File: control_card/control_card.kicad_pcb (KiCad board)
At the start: 2 copper layers, 27 parts, among them IC1 TLSR8253F512ET48, J1 Conn_02x04_Counter_Clockwise, U1 Wifi, Y1 Crystal_GND24_Small

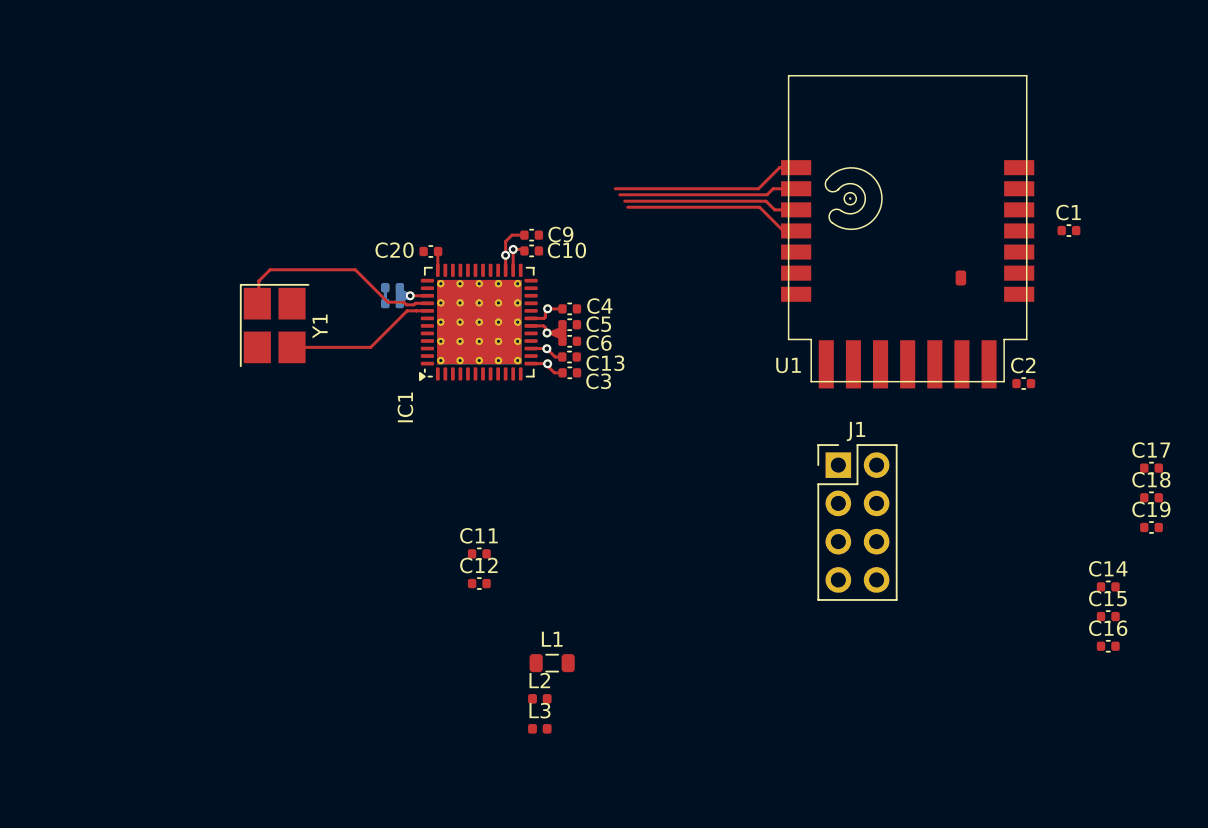
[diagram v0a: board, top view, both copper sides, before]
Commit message: PCB : started footprint and rooting
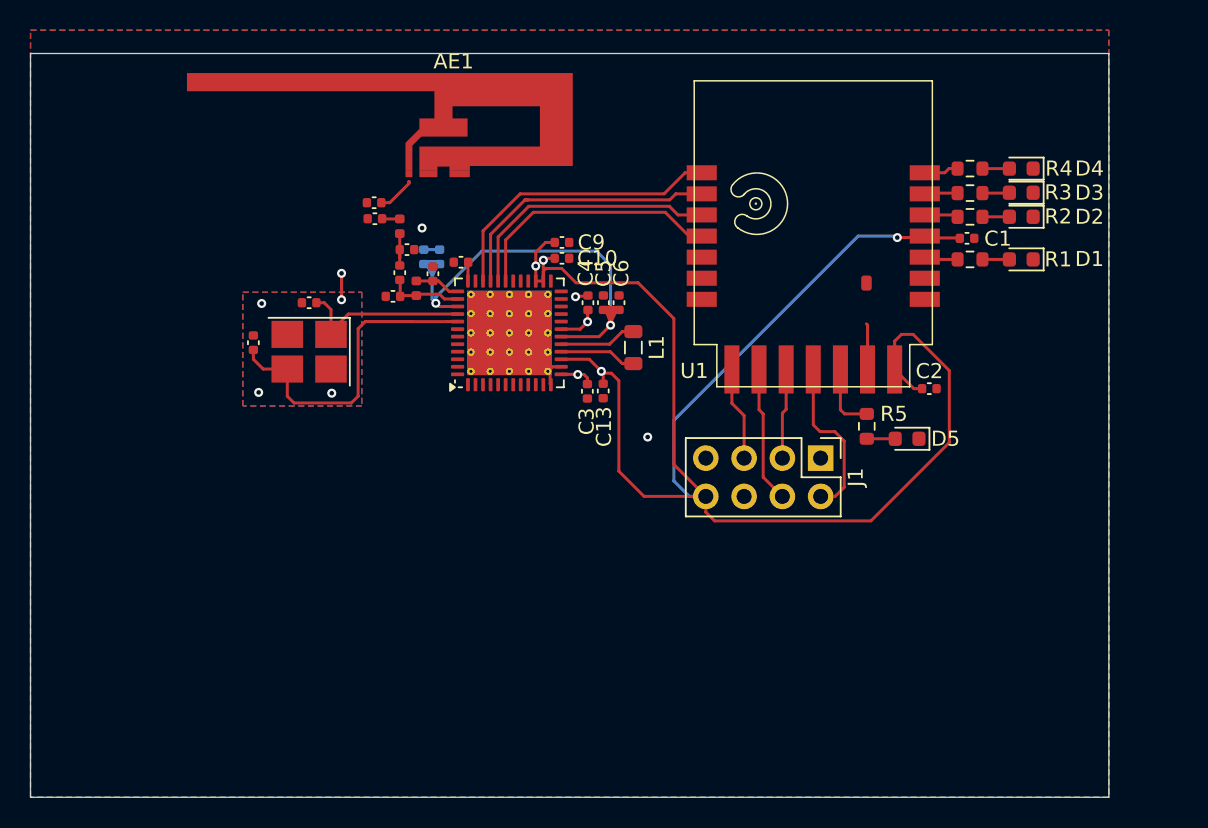
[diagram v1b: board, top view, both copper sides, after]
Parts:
- added AE1: Antenna, Footprint_Rang_Dong:Antenna, F.Cu at (73.0, 71.1)
- added D1: LED, LED_SMD:LED_0603_1608Metric, F.Cu at (110.6, 80.0)
- added D2: LED, LED_SMD:LED_0603_1608Metric, F.Cu at (110.6, 77.1)
- added D3: LED, LED_SMD:LED_0603_1608Metric, F.Cu at (110.6, 75.5)
- added D4: LED, LED_SMD:LED_0603_1608Metric, F.Cu at (110.6, 73.9)
- added D5: LED, LED_SMD:LED_0603_1608Metric, F.Cu at (103.1, 91.9)
- added R1: R, Resistor_SMD:R_0603_1608Metric, F.Cu at (107.2, 80.0)
- added R2: R, Resistor_SMD:R_0603_1608Metric, F.Cu at (107.2, 77.1)
- added R3: R, Resistor_SMD:R_0603_1608Metric, F.Cu at (107.2, 75.6)
- added R4: R, Resistor_SMD:R_0603_1608Metric, F.Cu at (107.2, 73.9)
- added R5: R, Resistor_SMD:R_0603_1608Metric, F.Cu at (100.4, 91.0)
- moved C19 55.9 mm to (67.7, 76.2), turned to 180 degrees
- moved C18 54.8 mm to (67.8, 77.3), turned to 180 degrees
- moved C16 53.1 mm to (69.4, 80.8), turned to 90 degrees
- moved C15 52.0 mm to (69.0, 82.4), turned to 180 degrees
- moved C17 51.5 mm to (69.9, 79.3)
- moved C14 49.4 mm to (71.6, 80.9), turned to 90 degrees
- moved L3 34.6 mm to (69.4, 77.8), turned to 90 degrees
- moved L2 28.4 mm to (70.5, 81.9), turned to 90 degrees
- moved C12 21.9 mm to (59.7, 85.5), turned to 90 degrees
- moved L1 21.6 mm to (84.9, 85.8), turned to -90 degrees
- moved C11 20.1 mm to (63.4, 82.8), turned to 180 degrees
- moved C1 6.78 mm to (107.0, 78.6)
- moved C2 6.27 mm to (104.5, 88.5)
- moved U1 6.27 mm to (88.9, 68.1)
- moved C8 4.40 mm to (72.0, 79.8), turned to 90 degrees
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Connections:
- net ANTENNA renamed Net-(AE1-A)
- U1 pad 10: CT1 -> CT3
- U1 pad 11: CT1 -> CT4
- U1 pad 9: CT1 -> CT2
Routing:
- net +3.3V: track 7.81 -> 111.3 mm, vias 3 -> 4
- net +1V2: track 6.13 -> 27.4 mm
- net Clock2: track 9.89 -> 21.3 mm
- net CT4: track 0.00 -> 11.1 mm
- net GND: track 0.00 -> 10.3 mm, vias 0 -> 8
- net CT2: track 0.00 -> 9.07 mm
- net In_1: track 12.6 -> 19.4 mm
- net In_2: track 11.9 -> 18.4 mm
- net CT1: track 0.00 -> 6.22 mm
- net CT3: track 0.00 -> 5.99 mm
- net In_3: track 11.6 -> 17.5 mm
- net In_4: track 11.8 -> 17.2 mm
- net Net-(IC1-VDCDC): track 0.00 -> 5.13 mm
- net Net-(IC1-VDCDC_SW): track 0.00 -> 5.11 mm
- net ANT: track 0.00 -> 5.10 mm
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- added copper zone on B.Cu, net GND
- added copper zone on F.Cu, net GND
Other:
- board outline added: 71.6 x 49.4 mm

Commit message: PCB (control_card): Almost Finished
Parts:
- AE1: value Antenna -> Antenna_Shield
- D1, D2, D3, D4, D5: footprint LED_SMD:LED_0603_1608Metric -> LED_SMD:LED_0805_2012Metric
- J1: moved to B.Cu
- moved J1 72.5 mm to (109.2, 21.6), turned to 90 degrees
- moved D5 61.3 mm to (89.2, 32.1), turned to 0 degrees
- moved R5 59.4 mm to (92.5, 32.1), turned to 180 degrees
- moved C15 51.8 mm to (73.4, 30.8), turned to 0 degrees
- moved U1 51.3 mm to (116.3, 24.7), turned to -90 degrees
- moved C16 50.6 mm to (71.9, 30.3)
- moved C18 50.6 mm to (71.4, 26.8)
- moved C19 50.6 mm to (71.4, 25.8)
- moved D1 50.5 mm to (89.2, 34.2), turned to 0 degrees
- moved L2 50.2 mm to (72.4, 31.8), turned to 0 degrees
- moved Y1 50.1 mm to (67.7, 36.2), turned to -90 degrees
- moved C17 49.7 mm to (73.4, 29.8)
- moved C2 49.6 mm to (96.7, 39.6), turned to 180 degrees
- moved L3 49.5 mm to (71.9, 28.3)
- moved C14 49.2 mm to (74.3, 31.8), turned to 0 degrees
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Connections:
- R1 pad 1: Led_1 -> Led_4
- R2 pad 1: Led_2 -> Led_3
- R3 pad 1: Led_3 -> Led_2
- R4 pad 1: Led_4 -> Led_1
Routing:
- net +3.3V: track 111.3 -> 156.5 mm, vias 4 -> 7
- net In_1: track 19.4 -> 40.1 mm, vias 0 -> 2
- net In_2: track 18.4 -> 38.3 mm, vias 0 -> 2
- net Led_4: track 2.29 -> 21.2 mm, vias 0 -> 2
- net In_3: track 17.5 -> 36.3 mm, vias 0 -> 2
- net In_4: track 17.2 -> 34.5 mm, vias 0 -> 2
- net CT4: track 11.1 -> 27.6 mm
- net Led_3: track 2.20 -> 18.7 mm, vias 0 -> 2
- net Led_2: track 2.23 -> 17.2 mm, vias 0 -> 2
- net Led_1: track 2.24 -> 14.6 mm, vias 0 -> 2
- net CT3: track 5.99 -> 17.2 mm
- net CT2: track 9.07 -> 17.8 mm
- net Clock2: track 21.3 -> 14.7 mm, vias 0 -> 2
- net CT1: track 6.22 -> 12.6 mm
- net GND: track 10.3 -> 5.25 mm, vias 8 -> 7
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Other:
- board size 71.6 x 49.4 mm -> 55.5 x 25.5 mm

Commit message: PCB (control_card) : V1 finished
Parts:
- moved C19 5.26 mm to (76.4, 27.5), turned to -90 degrees
- moved L2 4.68 mm to (70.4, 27.5), turned to -90 degrees
- moved C14 4.63 mm to (70.3, 29.5), turned to -90 degrees
- moved C18 3.95 mm to (75.3, 27.5), turned to -90 degrees
- moved C16 3.21 mm to (71.8, 27.1), turned to 0 degrees
- moved C15 3.02 mm to (71.3, 28.6), turned to -90 degrees
- moved L3 2.29 mm to (73.8, 27.1), turned to 0 degrees
- moved C17 1.62 mm to (72.3, 28.6), turned to -90 degrees
- moved AE1 0.89 mm to (81.6, 23.1)
- moved C11 0.81 mm to (64.9, 36.9)
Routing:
- net GND: track 5.25 -> 29.9 mm, vias 7 -> 11
- net ANT: track 7.72 -> 17.4 mm
- net VANT: track 5.33 -> 13.8 mm
- net Net-(AE1-A): track 2.08 -> 4.83 mm
- net +3.3V: track 156.5 -> 158.3 mm, vias 7 -> 6
- net CT1: track 12.6 -> 13.2 mm, vias 0 -> 1
- net VDD_F: track 2.66 -> 2.74 mm, vias 1 -> 0
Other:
- board size 55.5 x 25.5 mm -> 55.7 x 26.3 mm

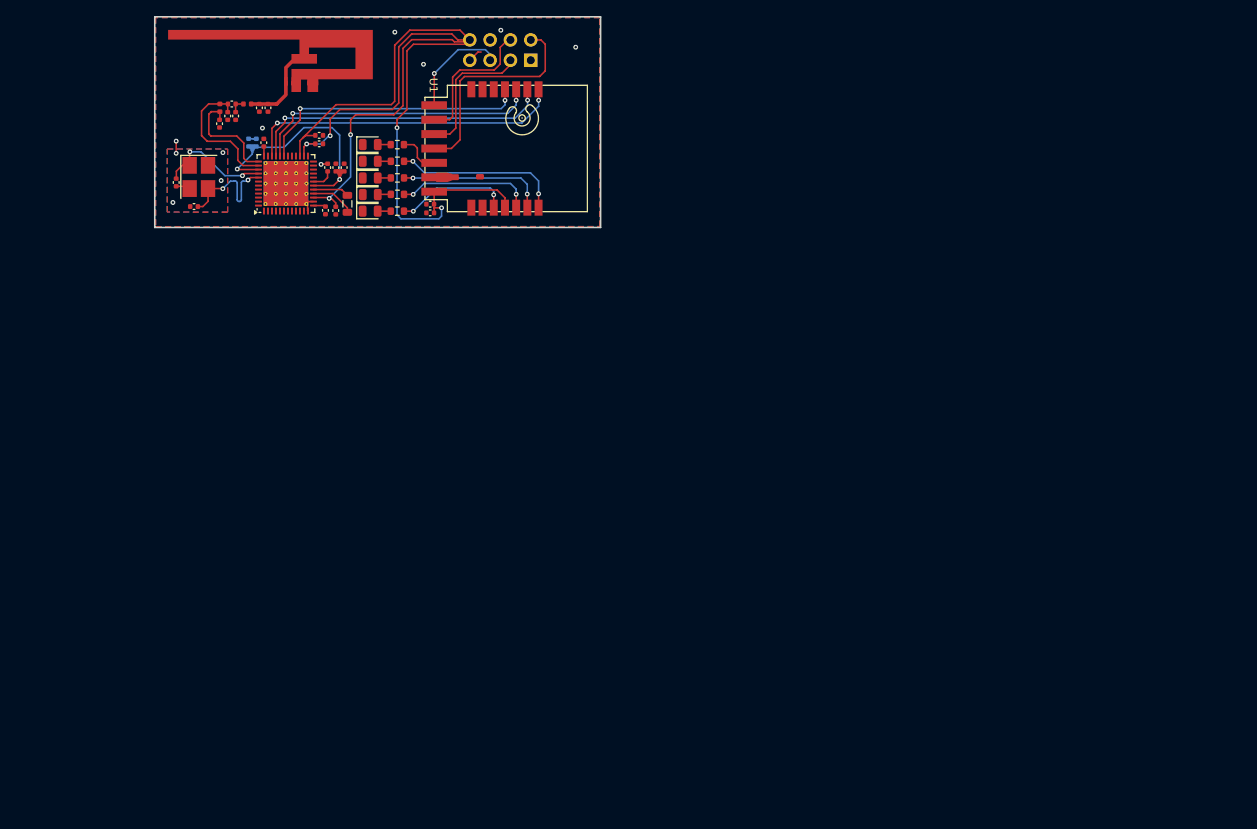
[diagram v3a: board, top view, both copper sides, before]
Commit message: PCB (control_card): V2 almost finished
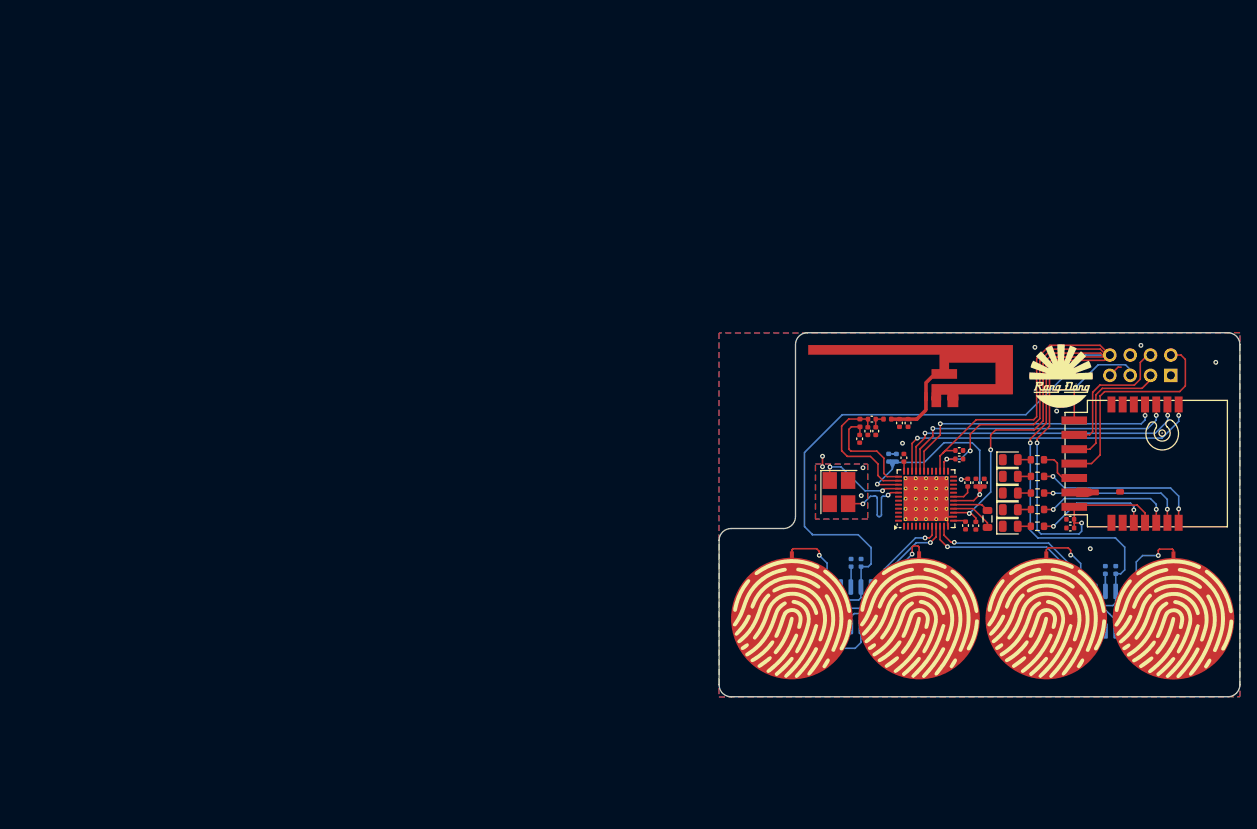
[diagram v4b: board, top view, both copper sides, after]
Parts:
- removed C11, C12: 1µF, Capacitor_SMD:C_0402_1005Metric
- added C21: 10nF, Capacitor_SMD:C_0402_1005Metric, B.Cu at (149.3, 84.4)
- added C22: 0.1µF, Capacitor_SMD:C_0402_1005Metric, B.Cu at (150.5, 84.4)
- added C24: 0.1µF, Capacitor_SMD:C_0402_1005Metric, B.Cu at (182.3, 85.3)
- added C25: 10nF, Capacitor_SMD:C_0402_1005Metric, B.Cu at (181.0, 85.3)
- added G***: LOGO, LOGO, F.Cu at (175.5, 61.1)
- added G***: LOGO, LOGO, F.Cu at (173.7, 91.4)
- added G***: LOGO, LOGO, F.Cu at (189.6, 91.4)
- added G***: LOGO, LOGO, F.Cu at (141.9, 91.4)
- added G***: LOGO, LOGO, F.Cu at (157.8, 91.4)
- added J2: Conn_01x01_Pin, Footprint_Rang_Dong:Touch-Pad, F.Cu at (141.9, 91.4)
- added J3: Conn_01x01_Pin, Footprint_Rang_Dong:Touch-Pad, F.Cu at (173.7, 91.4)
- added J4: Conn_01x01_Pin, Footprint_Rang_Dong:Touch-Pad, F.Cu at (157.8, 91.4)
- added J4: Conn_01x01_Pin, Footprint_Rang_Dong:Touch-Pad, F.Cu at (189.6, 91.4)
- added U2: ~, Package_SO:SOIC-8_3.9x4.9mm_P1.27mm, B.Cu at (149.9, 89.9)
- added U3: ~, Package_SO:SOIC-8_3.9x4.9mm_P1.27mm, B.Cu at (181.7, 90.4)
- moved C14 89.2 mm to (150.3, 68.9)
- moved C16 89.2 mm to (151.9, 66.4)
- moved C10 89.2 mm to (162.8, 71.4)
- moved C17 89.2 mm to (152.3, 67.9)
- moved C18 89.2 mm to (155.3, 66.9)
- moved C20 89.2 mm to (155.9, 71.3)
- moved C4 89.2 mm to (163.8, 74.4)
- moved C5 89.2 mm to (164.9, 74.4)
- moved C6 89.2 mm to (165.9, 74.4)
- moved C7 89.2 mm to (154.0, 71.3)
- moved C8 89.2 mm to (154.9, 71.3)
- moved C9 89.2 mm to (162.8, 70.4)
- moved D4 89.2 mm to (169.2, 79.8)
- moved L1 89.2 mm to (166.3, 78.9)
- moved L2 89.2 mm to (150.4, 66.9)
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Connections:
- IC1 pad 10: unconnected-(IC1-PB0-Pad10) -> Sig_4
- IC1 pad 11: unconnected-(IC1-PB1-Pad11) -> Sig_3
- IC1 pad 8: unconnected-(IC1-PA6-Pad8) -> Sig_2
- IC1 pad 9: unconnected-(IC1-PA7-Pad9) -> Sig_1
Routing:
- net +3.3V: track 158.3 -> 286.0 mm, vias 6 -> 7
- net Sig_3: track 0.00 -> 29.5 mm, vias 0 -> 1
- net Sig_4: track 0.00 -> 28.7 mm, vias 0 -> 1
- net Touch_2: track 0.00 -> 23.1 mm, vias 0 -> 1
- net Sig_2: track 0.00 -> 20.4 mm, vias 0 -> 1
- net Sig_1: track 0.00 -> 19.6 mm, vias 0 -> 1
- net Touch_4: track 0.00 -> 17.5 mm, vias 0 -> 1
- net Touch_3: track 0.00 -> 15.6 mm, vias 0 -> 1
- net Touch_1: track 0.00 -> 14.1 mm, vias 0 -> 1
- net Clock2: track 14.7 -> 11.6 mm
- net Clock1: track 14.7 -> 11.8 mm
- net Net-(U2-VC): track 0.00 -> 2.56 mm
- net Net-(U3-VC): track 0.00 -> 2.20 mm
- net GND: track 29.9 -> 28.3 mm
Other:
- board size 55.7 x 26.3 mm -> 65.1 x 45.5 mm

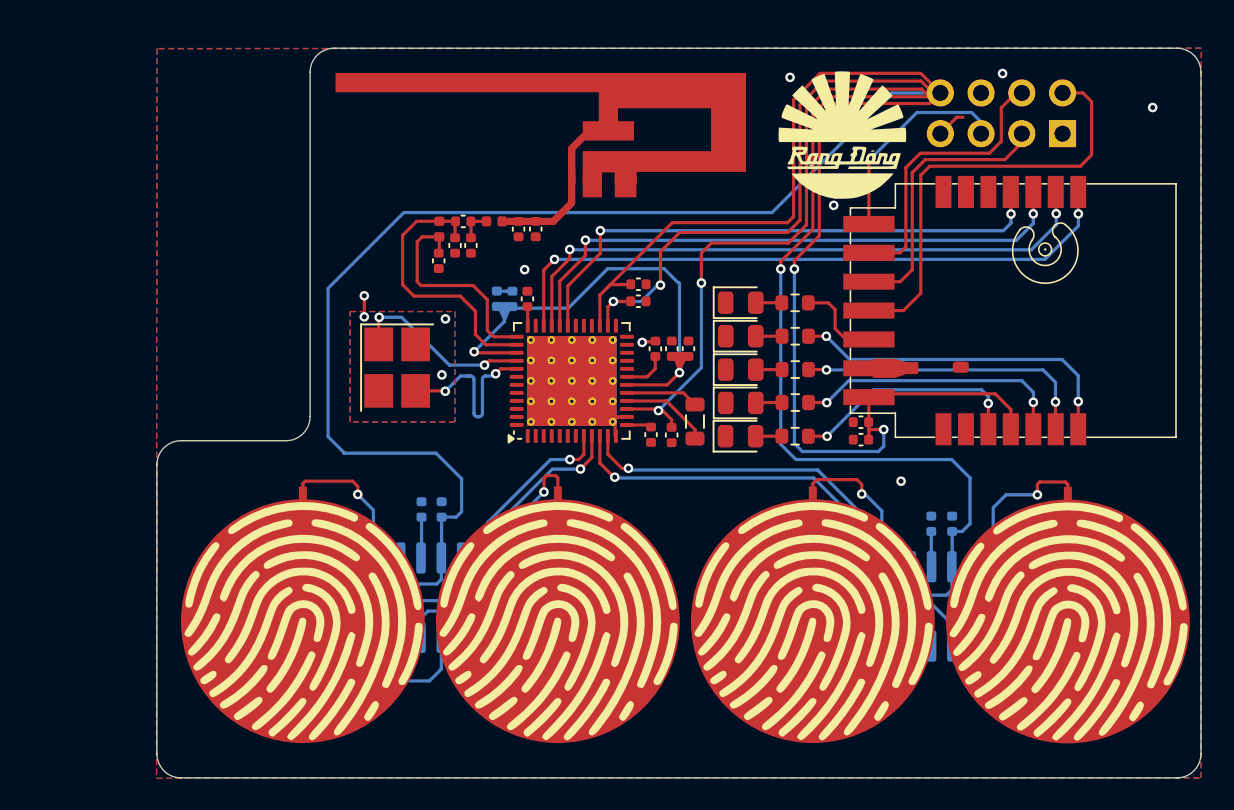
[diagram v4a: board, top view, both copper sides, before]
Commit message: PCB (control_card) : V3 finished, perfect dimension
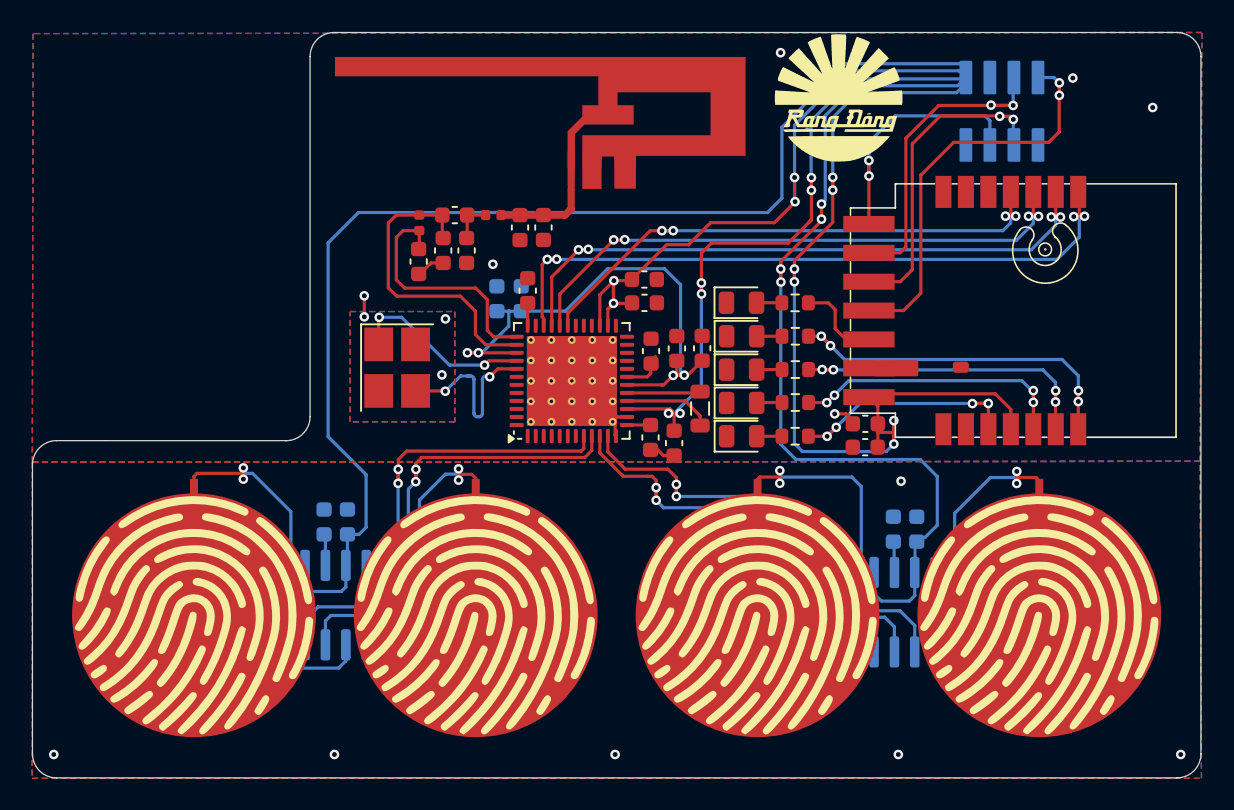
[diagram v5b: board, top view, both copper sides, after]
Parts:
- removed the G*** at (173.7, 91.4)
- removed the G*** at (189.6, 91.4)
- removed the G*** at (141.9, 91.4)
- removed the G*** at (157.8, 91.4)
- C1, C10, C13, C14, C15, C16, C17, C18, C19, C2, C20, C21, C22, C24, C25, C3, C4, C5, C6, C7, C8, C9: footprint Capacitor_SMD:C_0402_1005Metric -> Capacitor_SMD:C_0603_1608Metric
- J1: footprint Connector_PinHeader_2.54mm:PinHeader_2x04_P2.54mm_Vertical -> Footprint_Rang_Dong:Male connector
- moved J2 6.80 mm to (135.1, 91.0)
- moved C21 6.13 mm to (143.2, 85.2)
- moved U2 5.97 mm to (143.9, 90.4)
- moved C22 5.92 mm to (144.6, 85.2)
- moved J4 5.13 mm to (152.6, 91.0)
- moved J3 3.47 mm to (170.2, 91.0)
- moved C25 2.39 mm to (178.7, 85.6)
- moved U3 2.34 mm to (179.4, 90.8)
- moved G*** 2.33 mm to (175.3, 58.8)
- moved C24 2.23 mm to (180.1, 85.6)
- moved J5 1.82 mm to (187.8, 91.0)
- moved J1 1.68 mm to (187.7, 61.7), turned to 180 degrees
- moved L2 1.31 mm to (149.1, 66.5)
- moved C14 1.25 mm to (149.1, 68.9)
- moved AE1 0.99 mm to (161.5, 61.5)
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- renumbered J4 to J5
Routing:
- net +3.3V: track 286.0 -> 271.6 mm, vias 7 -> 20
- net Sig_2: track 20.4 -> 29.8 mm, vias 1 -> 2
- net Sig_1: track 19.6 -> 28.6 mm, vias 1 -> 2
- net Touch_4: track 17.5 -> 21.5 mm, vias 1 -> 2
- net +1V2: track 29.6 -> 33.5 mm, vias 2 -> 4
- net CT3: track 17.2 -> 20.6 mm, vias 0 -> 2
- net In_1: track 40.1 -> 43.3 mm, vias 2 -> 4
- net Sig_4: track 28.7 -> 25.6 mm, vias 1 -> 2
- net Touch_1: track 14.1 -> 16.9 mm, vias 1 -> 2
- net CT1: track 13.2 -> 16.0 mm, vias 1 -> 2
- net Sig_3: track 29.5 -> 26.7 mm, vias 1 -> 2
- net CT2: track 17.8 -> 19.9 mm, vias 0 -> 2
- net ANT: track 17.4 -> 19.4 mm
- net Touch_3: track 15.6 -> 17.4 mm, vias 1 -> 2
- net VANT: track 13.8 -> 15.5 mm
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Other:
- board size 65.1 x 45.5 mm -> 72.9 x 46.5 mm

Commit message: PCB (control_card): ready for review
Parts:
- moved G*** 0.60 mm to (175.0, 59.3)
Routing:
- net Clock2: track 11.6 -> 14.6 mm, vias 2 -> 0
- net Clock1: track 11.8 -> 13.4 mm, vias 2 -> 4
- net CT1: track 16.0 -> 16.6 mm
